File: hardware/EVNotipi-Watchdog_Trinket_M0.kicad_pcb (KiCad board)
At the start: 2 copper layers, 25 x 34 mm, 11 parts, among them J1 Conn_Left, J2 Conn_Right, J3 Conn_Pi, J4 Conn_Pwr, J5 Conn_01x04_Male, Q1 BS170, Q2 IRF5305, U1 TSR_2-2450

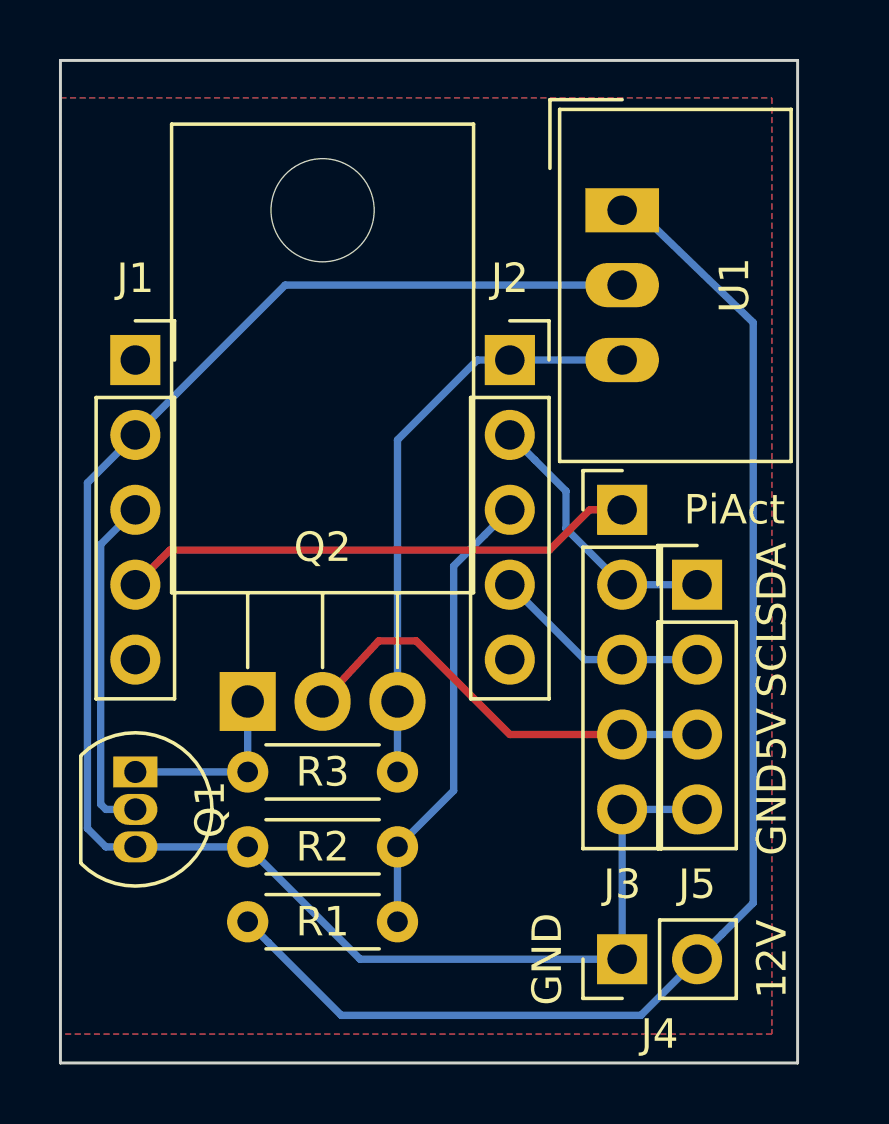
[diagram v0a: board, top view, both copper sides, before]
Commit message: give the resistors and the TSR2-2450 more space
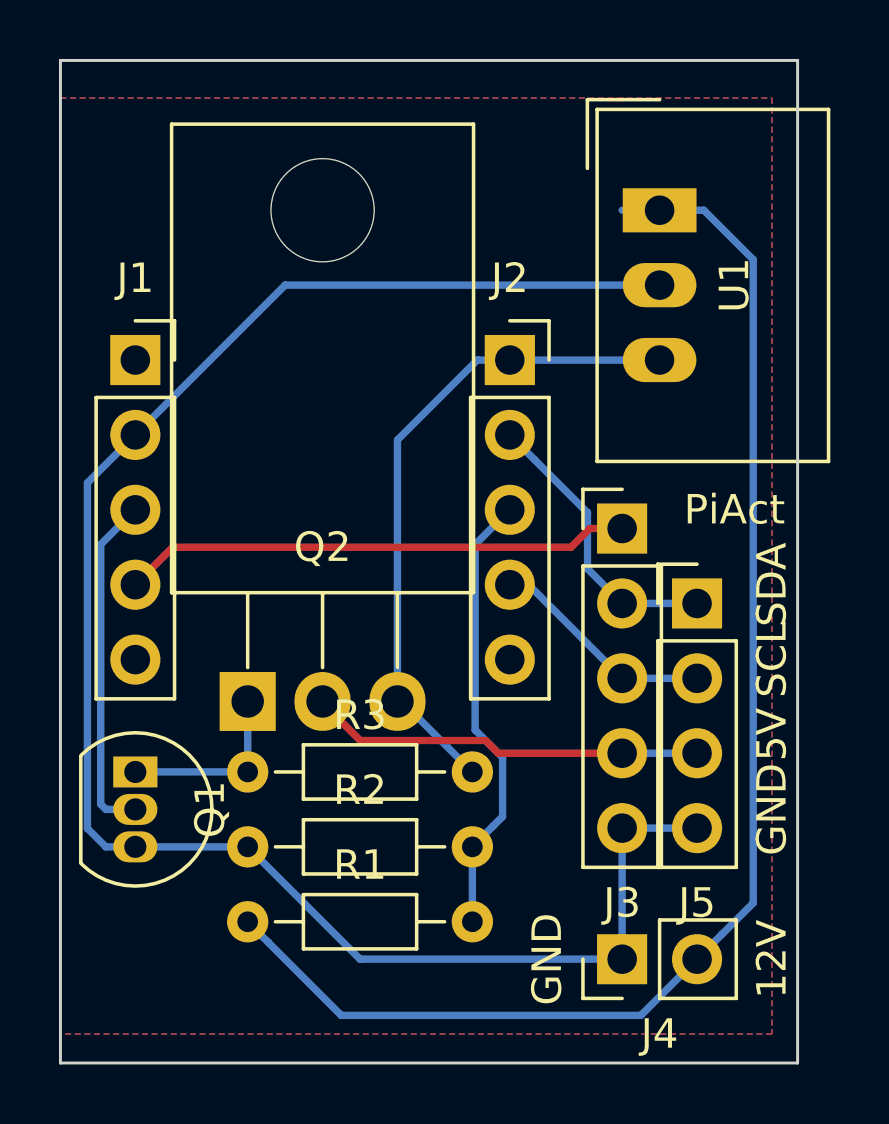
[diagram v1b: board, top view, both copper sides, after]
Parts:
- R1, R2: footprint Resistor_THT:R_Axial_DIN0204_L3.6mm_D1.6mm_P5.08mm_Horizontal -> Resistor_THT:R_Axial_DIN0204_L3.6mm_D1.6mm_P7.62mm_Horizontal
- R3: value R22K -> R27K; footprint Resistor_THT:R_Axial_DIN0204_L3.6mm_D1.6mm_P5.08mm_Horizontal -> Resistor_THT:R_Axial_DIN0204_L3.6mm_D1.6mm_P7.62mm_Horizontal
- moved U1 1.27 mm to (74.9, 35.6)
- moved J5 0.64 mm to (76.2, 48.9)
- moved J3 0.63 mm to (73.7, 46.4)
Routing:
- net VCC5V: track 20.0 -> 22.4 mm
- net VCC_Pi: track 14.9 -> 13.5 mm
- net GND: track 60.2 -> 60.9 mm
- net SDA: track 9.20 -> 9.83 mm
- net VCC12V: track 45.7 -> 46.2 mm
